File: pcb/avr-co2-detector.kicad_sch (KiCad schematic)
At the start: 62 parts, among them J1 USB TYPE-C, J2 Backlight, J3 Backlight, J4 LCD0802, J5 AVR-ISP-10, J6 BH1.27-6-2, SW1 "Reset", SW2 "Reset", SW3 "Config", U1 ATtiny2313A-SU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

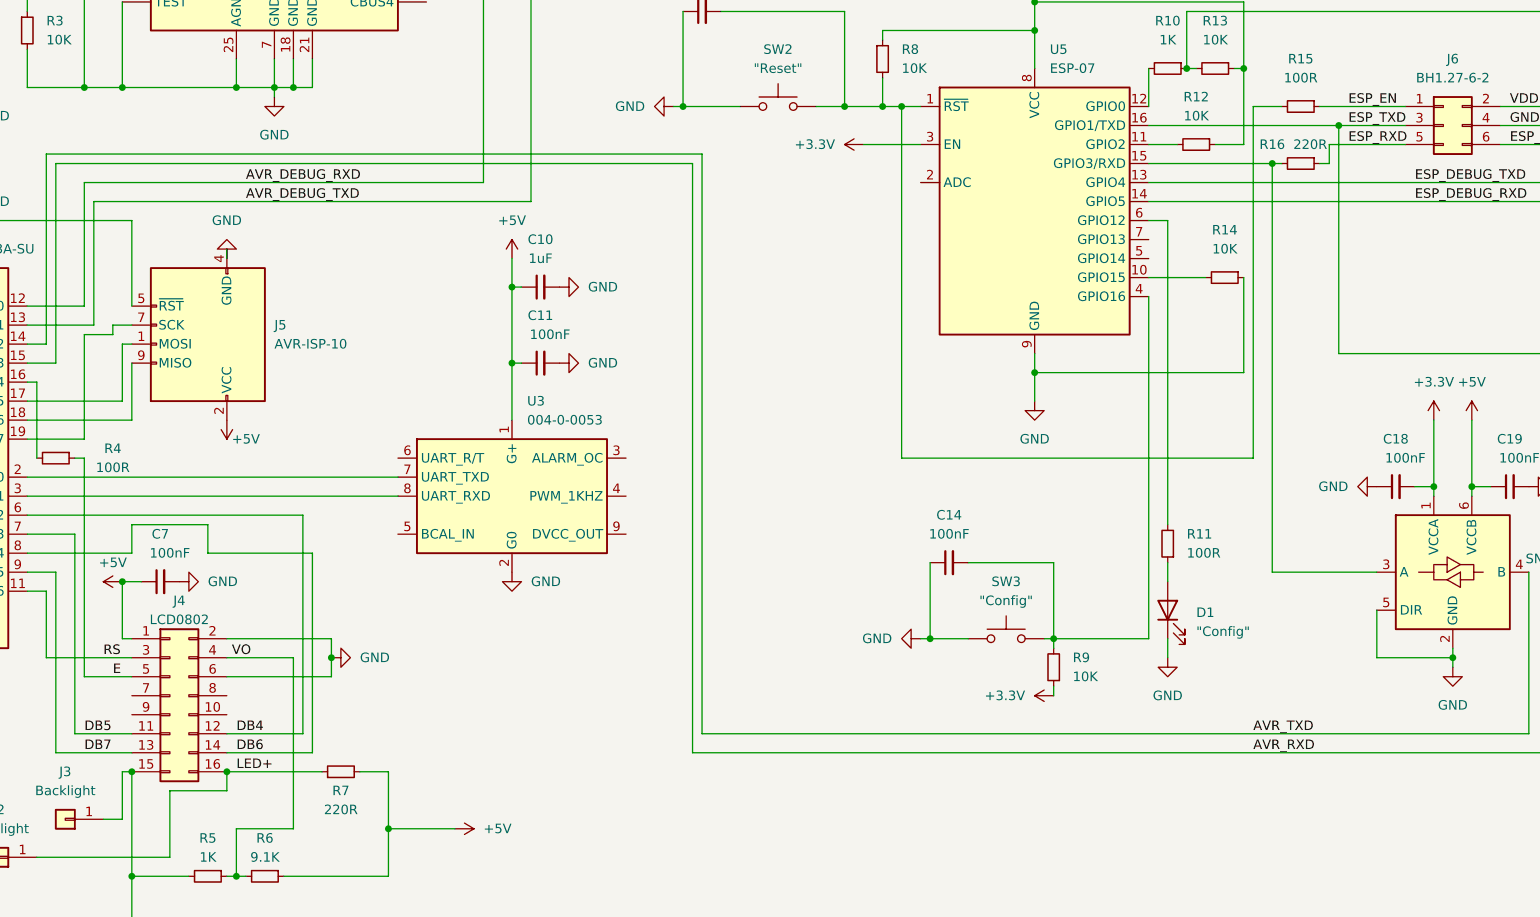
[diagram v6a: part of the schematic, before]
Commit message: Fixed LCD connector pinout, corrected resistor R16 connection
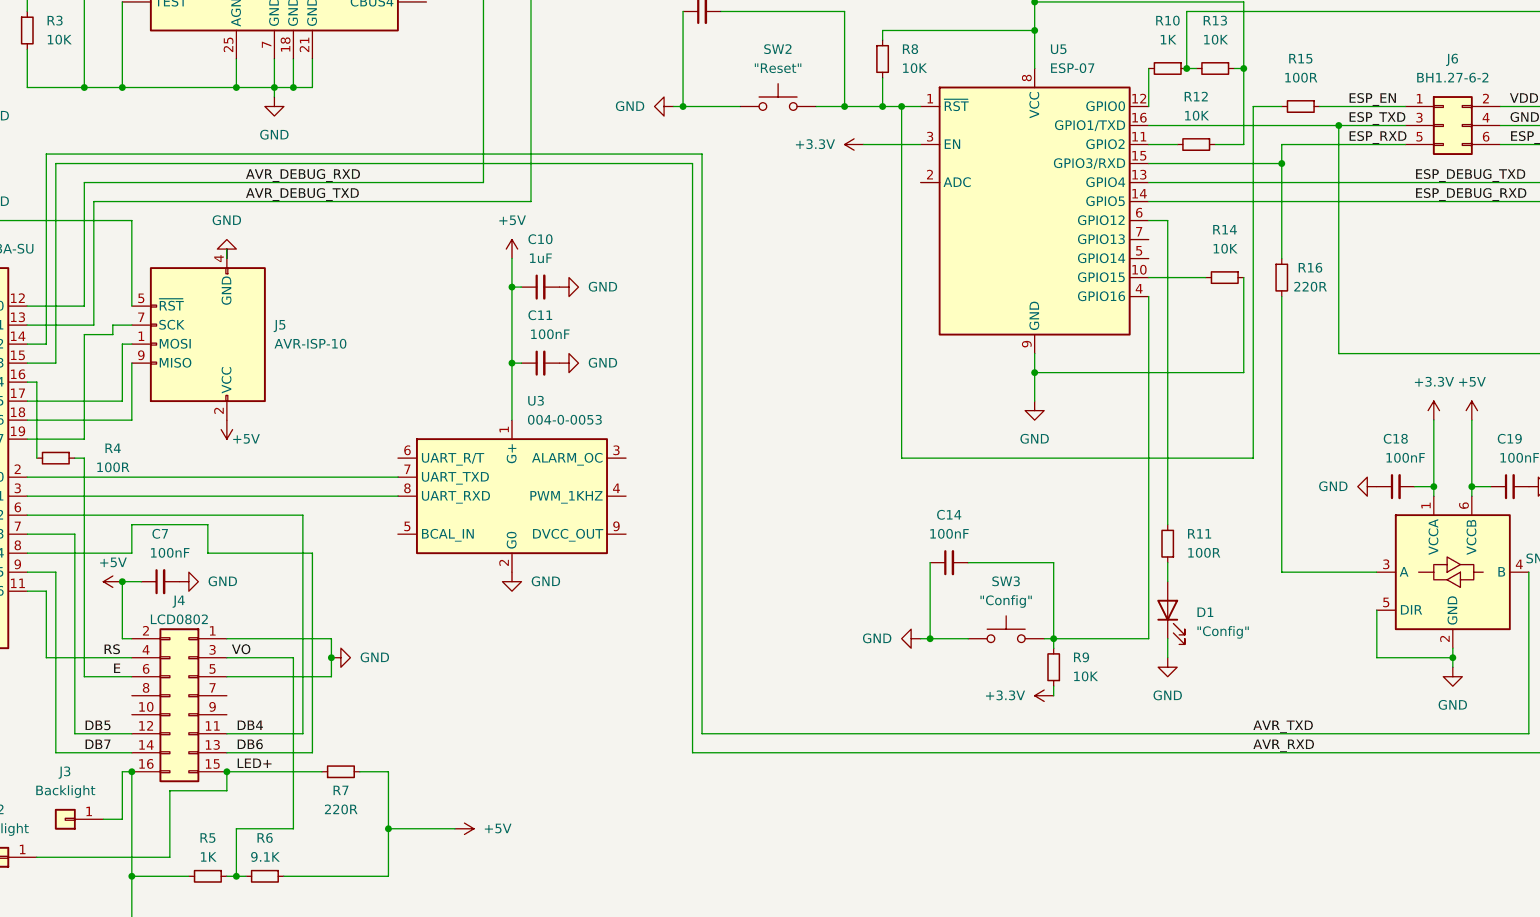
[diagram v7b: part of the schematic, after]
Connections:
- net +5V: now also J4.2 (Pin_2); no longer J4.1 (Pin_1)
- net DB4: now also J4.11 (Pin_11); no longer J4.12 (Pin_12)
- net DB5: now also J4.12 (Pin_12); no longer J4.11 (Pin_11)
- net DB6: now also J4.13 (Pin_13); no longer J4.14 (Pin_14)
- net DB7: now also J4.14 (Pin_14); no longer J4.13 (Pin_13)
- net E: now also J4.6 (Pin_6); no longer J4.5 (Pin_5)
- net ESP_RXD: now also U5.15 (GPIO3/RXD)
- net GND: now also J4.1 (Pin_1), J4.16 (Pin_16), J4.5 (Pin_5); no longer J4.15 (Pin_15), J4.2 (Pin_2), J4.6 (Pin_6)
- net LED+: now also J4.15 (Pin_15); no longer J4.16 (Pin_16)
- net RS: now also J4.4 (Pin_4); no longer J4.3 (Pin_3)
- net VO: now also J4.3 (Pin_3); no longer J4.4 (Pin_4)
- net at R16.2, U6.3 (A): no longer U5.15 (GPIO3/RXD)
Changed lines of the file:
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@@
   (junction (at 344.17 142.24) (diameter 0) (color 0 0 0 0)
   )
+  (junction (at 267.97 101.6) (diameter 0) (color 0 0 0 0)
+  )
   (junction (at 58.42 133.35) (diameter 0) (color 0 0 0 0)
   )
@@
   (junction (at 114.3 182.88) (diameter 0) (color 0 0 0 0)
   )
-  (junction (at 266.7 101.6) (diameter 0) (color 0 0 0 0)
-  )
   (junction (at 339.09 146.05) (diameter 0) (color 0 0 0 0)
   )
@@
     (stroke (width 0) (type default) (color 0 0 0 0))
   )
+  (wire (pts (xy 267.97 119.38) (xy 267.97 156.21))
+    (stroke (width 0) (type default) (color 0 0 0 0))
+  )
   (wire (pts (xy 234.95 66.04) (xy 234.95 77.47))
     (stroke (width 0) (type default) (color 0 0 0 0))
@@
     (stroke (width 0) (type default) (color 0 0 0 0))
   )
-  (wire (pts (xy 266.7 101.6) (xy 267.97 101.6))
-    (stroke (width 0) (type default) (color 0 0 0 0))
-  )
   (wire (pts (xy 156.21 44.45) (xy 161.29 44.45))
     (stroke (width 0) (type default) (color 0 0 0 0))
@@
     (stroke (width 0) (type default) (color 0 0 0 0))
   )
+  (wire (pts (xy 267.97 101.6) (xy 267.97 114.3))
+    (stroke (width 0) (type default) (color 0 0 0 0))
+  )
   (wire (pts (xy 128.27 190.5) (xy 128.27 196.85))
     (stroke (width 0) (type default) (color 0 0 0 0))
@@
     (stroke (width 0) (type default) (color 0 0 0 0))
   )
+  (wire (pts (xy 267.97 99.06) (xy 267.97 101.6))
+    (stroke (width 0) (type default) (color 0 0 0 0))
+  )
   (wire (pts (xy 234.95 129.54) (xy 234.95 127))
     (stroke (width 0) (type default) (color 0 0 0 0))
@@
     (stroke (width 0) (type default) (color 0 0 0 0))
   )
-  (wire (pts (xy 107.95 170.18) (xy 114.3 170.18))
-    (stroke (width 0) (type default) (color 0 0 0 0))
-  )
   (wire (pts (xy 85.09 95.25) (xy 85.09 106.68))
     (stroke (width 0) (type default) (color 0 0 0 0))
@@
     (stroke (width 0) (type default) (color 0 0 0 0))
   )
-  (wire (pts (xy 266.7 101.6) (xy 266.7 156.21))
-    (stroke (width 0) (type default) (color 0 0 0 0))
-  )
   (wire (pts (xy 135.89 91.44) (xy 138.43 91.44))
     (stroke (width 0) (type default) (color 0 0 0 0))
@@
     (stroke (width 0) (type default) (color 0 0 0 0))
   )
-  (wire (pts (xy 274.32 101.6) (xy 274.32 99.06))
-    (stroke (width 0) (type default) (color 0 0 0 0))
-  )
   (wire (pts (xy 113.03 165.1) (xy 113.03 157.48))
     (stroke (width 0) (type default) (color 0 0 0 0))
@@
     (stroke (width 0) (type default) (color 0 0 0 0))
   )
-  (wire (pts (xy 280.67 156.21) (xy 266.7 156.21))
+  (wire (pts (xy 280.67 156.21) (xy 267.97 156.21))
     (stroke (width 0) (type default) (color 0 0 0 0))
   )
@@
     (stroke (width 0) (type default) (color 0 0 0 0))
   )
+  (wire (pts (xy 107.95 170.18) (xy 114.3 170.18))
+    (stroke (width 0) (type default) (color 0 0 0 0))
+  )
   (wire (pts (xy 38.1 114.3) (xy 45.72 114.3))
     (stroke (width 0) (type default) (color 0 0 0 0))
@@
     (stroke (width 0) (type default) (color 0 0 0 0))
   )
-  (wire (pts (xy 273.05 101.6) (xy 274.32 101.6))
-    (stroke (width 0) (type default) (color 0 0 0 0))
-  )
   (wire (pts (xy 107.95 120.65) (xy 107.95 104.14))
     (stroke (width 0) (type default) (color 0 0 0 0))
@@
     (stroke (width 0) (type default) (color 0 0 0 0))
   )
-  (wire (pts (xy 250.19 101.6) (xy 266.7 101.6))
+  (wire (pts (xy 250.19 101.6) (xy 267.97 101.6))
     (stroke (width 0) (type default) (color 0 0 0 0))
   )
@@
     (stroke (width 0) (type default) (color 0 0 0 0))
   )
-  (wire (pts (xy 274.32 99.06) (xy 284.48 99.06))
+  (wire (pts (xy 267.97 99.06) (xy 284.48 99.06))
     (stroke (width 0) (type default) (color 0 0 0 0))
   )
@@
     (pin "2")
   )
-  (symbol (lib_id "Device:R_Small") (at 270.51 101.6 270) (unit 1)
-    (in_bom yes) (on_board yes)
-    (property "Reference" "R16" (id 0) (at 266.7 99.06 90))
-    (property "Value" "220R" (id 1) (at 271.78 99.06 90))
-    (property "Footprint" "Resistor_SMD:R_0805_2012Metric_Pad1.20x1.40mm_HandSolder" (id 2) (at 270.51 101.6 0)
-      (effects (font (size 1.27 1.27)) hide)
-    )
-    (property "Datasheet" "~" (id 3) (at 270.51 101.6 0)
-      (effects (font (size 1.27 1.27)) hide)
-    )
-    (pin "1")
-    (pin "2")
-  )
   (symbol (lib_id "Connector_Generic:Conn_01x01") (at 105.41 189.23 180) (unit 1)
     (in_bom yes) (on_board yes) (fields_autoplaced)
@@
     (pin "1")
   )
-  (symbol (lib_id "Connector_Generic:Conn_02x08_Odd_Even") (at 119.38 172.72 0) (unit 1)
+  (symbol (lib_id "Connector_Generic:Conn_02x08_Odd_Even") (at 121.92 172.72 0) (mirror y) (unit 1)
     (in_bom yes) (on_board yes)
     (property "Reference" "J4" (id 0) (at 120.65 160.02 0))
     (property "Value" "LCD0802" (id 1) (at 120.65 162.56 0))
-    (property "Footprint" "Connector_IDC:IDC-Header_2x08_P2.54mm_Vertical" (id 2) (at 119.38 172.72 0)
+    (property "Footprint" "Connector_IDC:IDC-Header_2x08_P2.54mm_Vertical" (id 2) (at 121.92 172.72 0)
       (effects (font (size 1.27 1.27)) hide)
     )
-    (property "Datasheet" "~" (id 3) (at 119.38 172.72 0)
+    (property "Datasheet" "~" (id 3) (at 121.92 172.72 0)
       (effects (font (size 1.27 1.27)) hide)
     )
@@
   (symbol (lib_id "power:+3.3V") (at 237.49 172.72 90) (unit 1)
     (in_bom yes) (on_board yes) (fields_autoplaced)
-    (property "Reference" "#PWR?" (id 0) (at 241.3 172.72 0)
+    (property "Reference" "#PWR0101" (id 0) (at 241.3 172.72 0)
       (effects (font (size 1.27 1.27)) hide)
     )
@@
     (pin "3")
   )
+  (symbol (lib_id "Device:R_Small") (at 267.97 116.84 0) (unit 1)
+    (in_bom yes) (on_board yes)
+    (property "Reference" "R16" (id 0) (at 271.78 115.57 0))
+    (property "Value" "220R" (id 1) (at 271.78 118.11 0))
+    (property "Footprint" "Resistor_SMD:R_0805_2012Metric_Pad1.20x1.40mm_HandSolder" (id 2) (at 267.97 116.84 0)
+      (effects (font (size 1.27 1.27)) hide)
+    )
+    (property "Datasheet" "~" (id 3) (at 267.97 116.84 0)
+      (effects (font (size 1.27 1.27)) hide)
+    )
+    (pin "1")
+    (pin "2")
+  )
   (symbol (lib_id "Connector_Generic:Conn_02x03_Odd_Even") (at 289.56 96.52 0) (unit 1)
     (in_bom yes) (on_board yes) (fields_autoplaced)
@@
     )
     (path "/3ce18ad5-c25f-473d-96d7-76d865186ed1"
-      (reference "#PWR?") (unit 1) (value "+3.3V") (footprint "")
+      (reference "#PWR0101") (unit 1) (value "+3.3V") (footprint "")
     )
     (path "/9027a3cb-d61e-47fa-a79d-fba2d8e0022e"
@@
       (reference "R15") (unit 1) (value "100R") (footprint "Resistor_SMD:R_0805_2012Metric_Pad1.20x1.40mm_HandSolder")
     )
-    (path "/09a93844-90f2-469e-82e8-a867b25e01c2"
+    (path "/7314d098-387a-4bbe-813f-951ac2b119a7"
       (reference "R16") (unit 1) (value "220R") (footprint "Resistor_SMD:R_0805_2012Metric_Pad1.20x1.40mm_HandSolder")
     )

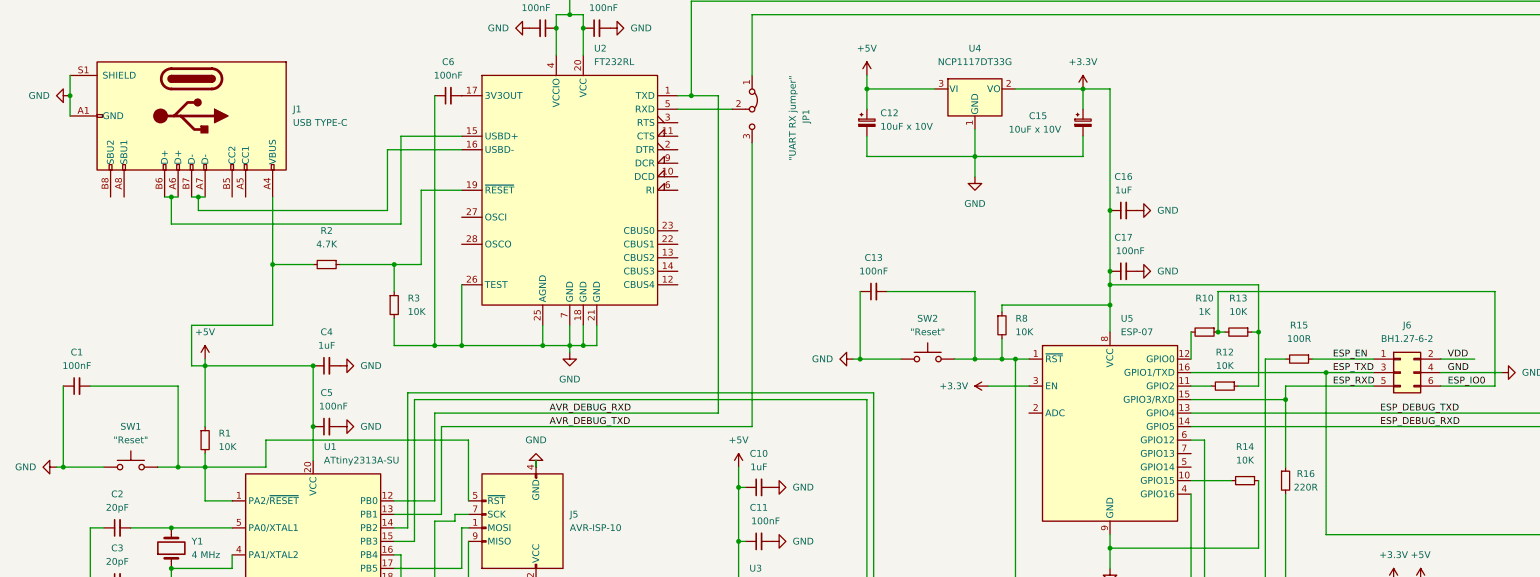
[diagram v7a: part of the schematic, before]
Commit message: Increased width of traces of 3.3V and 5V, mirrored project info on silkscreen, added "Debug UART" connector
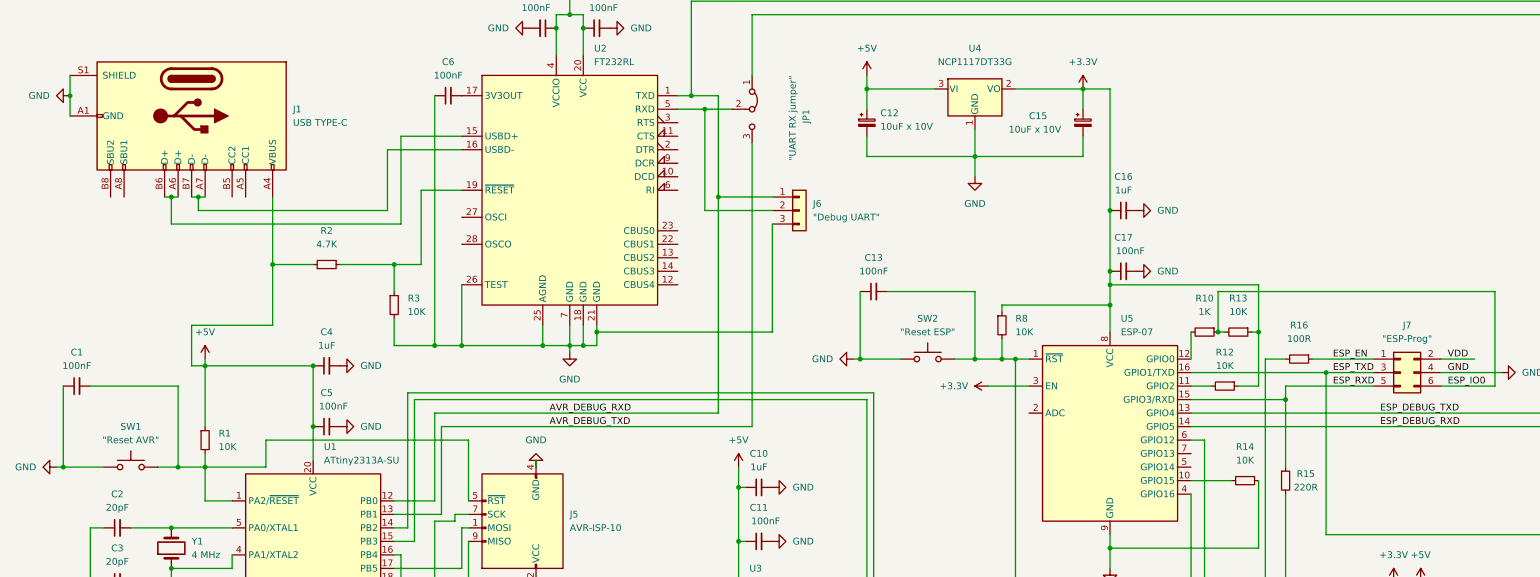
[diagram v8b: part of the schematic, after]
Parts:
- added J6: "Debug UART", Connector_PinHeader_2.54mm:PinHeader_1x03_P2.54mm_Vertical, symbol Connector_Generic:Conn_01x03
- J7: renamed from J6; value BH1.27-6-2 -> "ESP-Prog"
- SW1: value "Reset" -> "Reset AVR"
- SW2: value "Reset" -> "Reset ESP"
- renumbered R16 to R15, R15 to R16
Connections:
- net AVR_DEBUG_RXD: now also J6.1 (Pin_1)
- net GND: now also J6.3 (Pin_3)
- net at JP1.2 (C), U2.5 (RXD): now also J6.2 (Pin_2)
